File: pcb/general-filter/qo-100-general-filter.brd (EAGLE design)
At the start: 51 x 20 mm, 35 parts

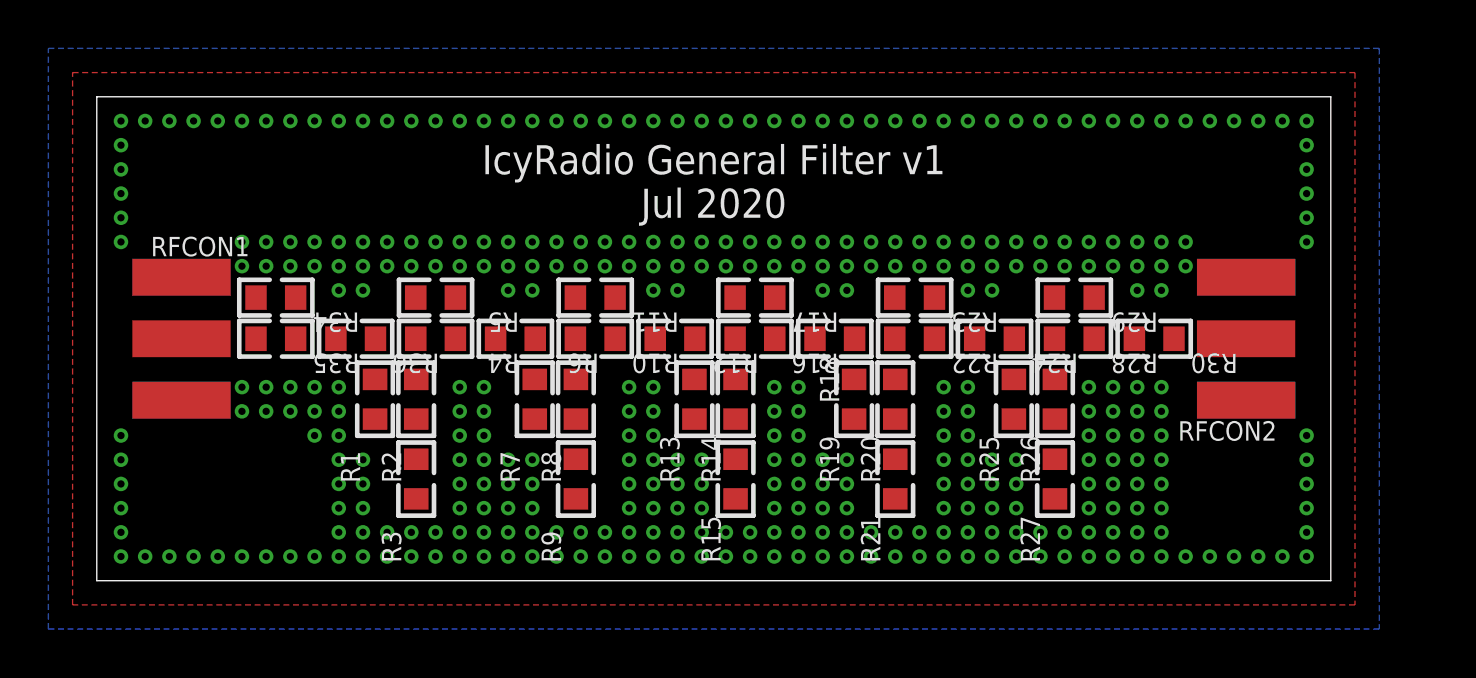
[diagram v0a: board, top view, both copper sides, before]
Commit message: Finish general filter PCB Fix screw not connected to GND on upconverter PCB Some work on upconverter software
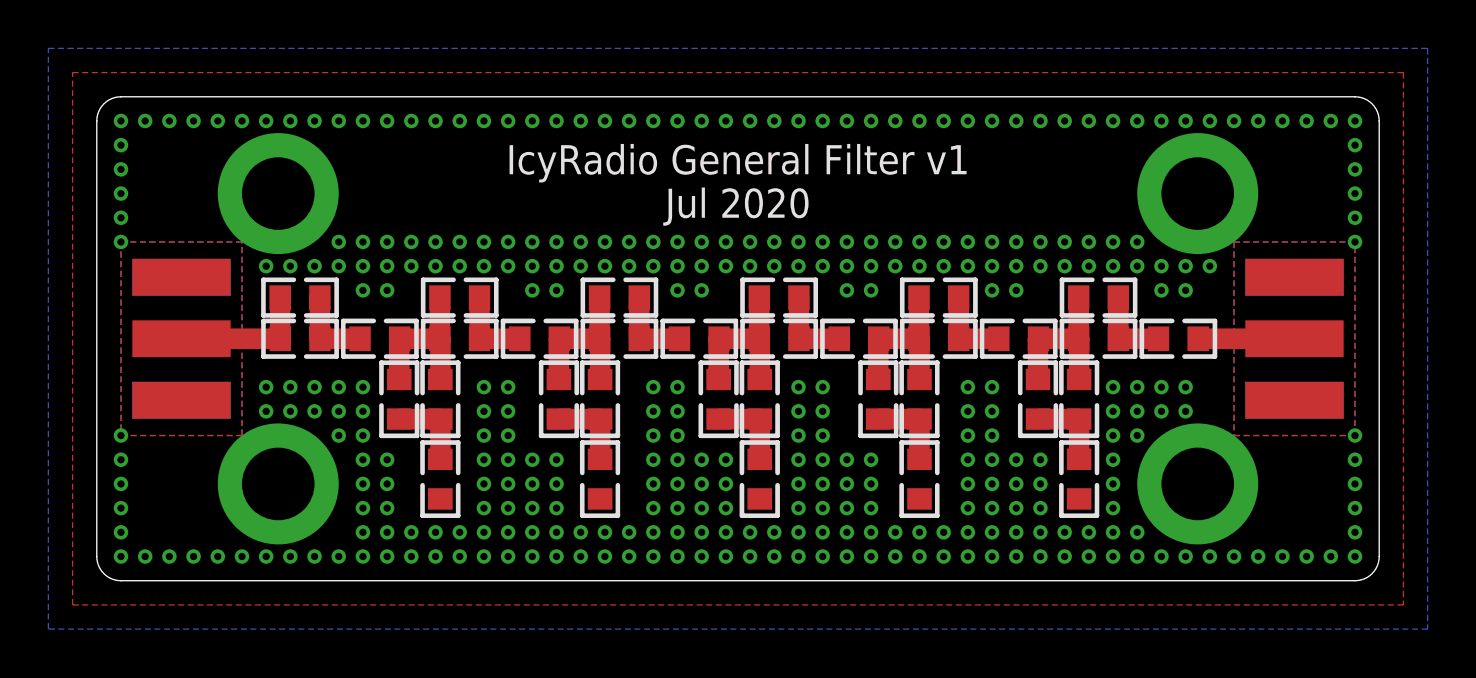
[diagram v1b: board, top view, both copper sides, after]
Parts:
- moved RFCON2 2.00 mm to (49.5, 10.0)
- moved R1 1.00 mm to (12.5, 7.50)
- moved R10 1.00 mm to (21.6, 10.0)
- moved R11 1.00 mm to (21.6, 11.7)
- moved R12 1.00 mm to (24.9, 10.0)
- moved R13 1.00 mm to (25.7, 7.50)
- moved R14 1.00 mm to (27.4, 7.50)
- moved R15 1.00 mm to (27.4, 4.20)
- moved R16 1.00 mm to (28.2, 10.0)
- moved R17 1.00 mm to (28.2, 11.7)
- moved R18 1.00 mm to (31.5, 10.0)
- moved R2 1.00 mm to (14.2, 7.50)
- moved R20 1.00 mm to (34.0, 7.50)
- moved R21 1.00 mm to (34.0, 4.20)
- moved R22 1.00 mm to (34.8, 10.0)
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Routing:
- net N$13: track 0.00 -> 6.74 mm
- net N$10: track 0.00 -> 6.74 mm
- net N$7: track 0.00 -> 6.74 mm
- net N$3: track 0.00 -> 6.74 mm
- net N$1: track 0.00 -> 6.74 mm
- net N$18: track 0.00 -> 5.78 mm
- net N$16: track 0.00 -> 3.98 mm
- net N$14: track 0.00 -> 3.36 mm
- net N$11: track 0.00 -> 3.36 mm
- net N$6: track 0.00 -> 3.36 mm
- net N$15: track 0.00 -> 3.36 mm
- net N$12: track 0.00 -> 3.36 mm
- net N$8: track 0.00 -> 3.36 mm
- net N$5: track 0.00 -> 3.36 mm
- net N$2: track 0.00 -> 3.36 mm
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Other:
- board size 51 x 20 mm -> 53 x 20 mm
